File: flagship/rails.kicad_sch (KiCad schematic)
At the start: 58 parts, among them U5 TPS54560B 12V, U6 TPS54560B 5V, U7 TPS54560B 3V3

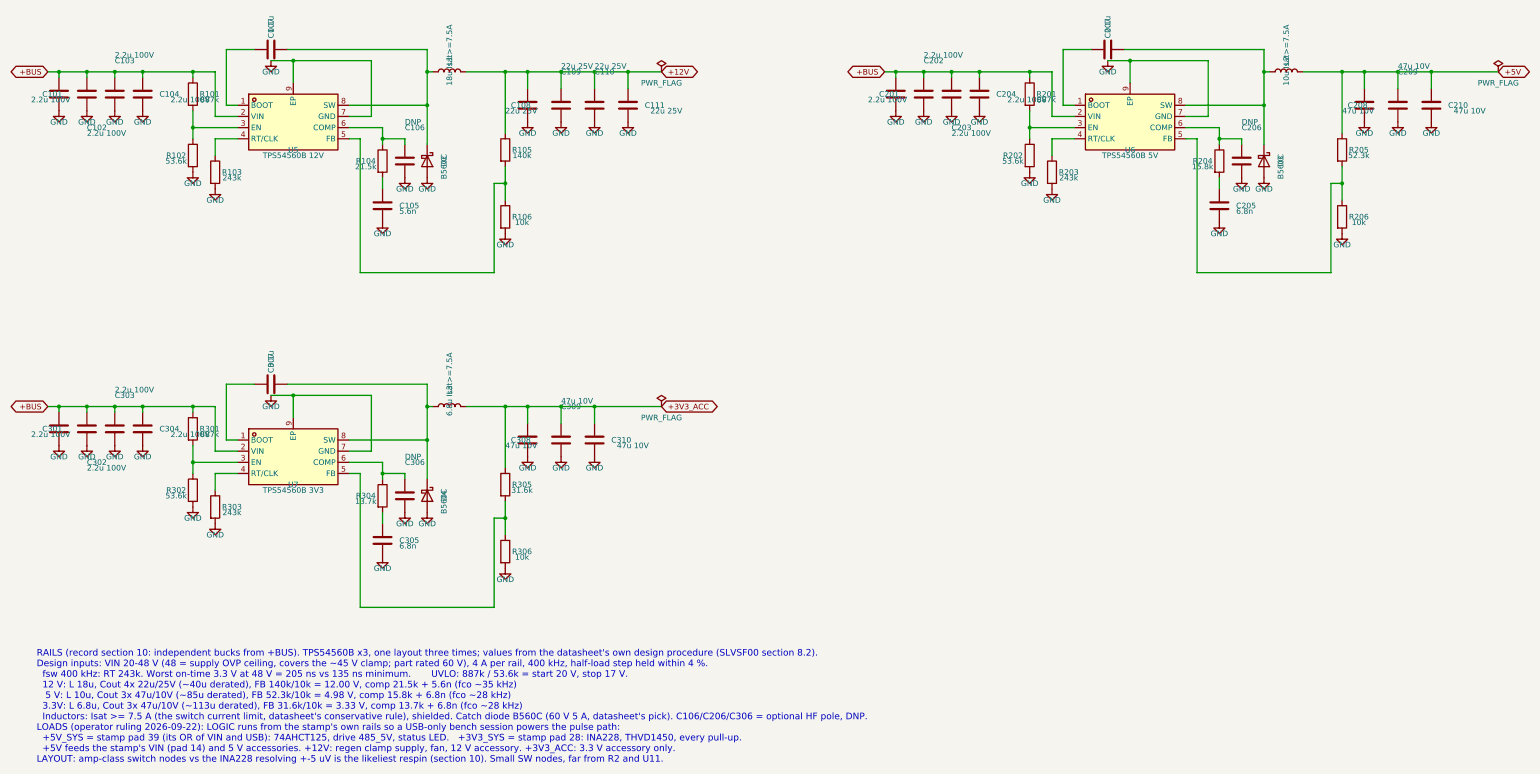
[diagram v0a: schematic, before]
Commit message: flagship: Kelvin WSK2512 shunts everywhere (LTC4364 sense now 4-terminal), bulk and MLCC parts picked
R1 (LTC4364, 2.5 mOhm) becomes a 4-terminal shunt with SENSE and OUT on its Kelvin taps;
R1/R2/R401 all Vishay WSK2512 on the T2.21 mm footprint that value range needs. Bulk:
2x EEH-ZA1J101P 100 uF 63 V hybrid polymer + 2x GRM32ER72A225KA35L; buck input caps get
the same MLCC part number. Regen resistors labeled D2TO35M 24 R 2 %. Input nets verified
exact after regeneration; ERC 0 on every detailed sheet.

Co-Authored-By: Claude Opus 5.5 (1M context) <noreply@anthropic.com>
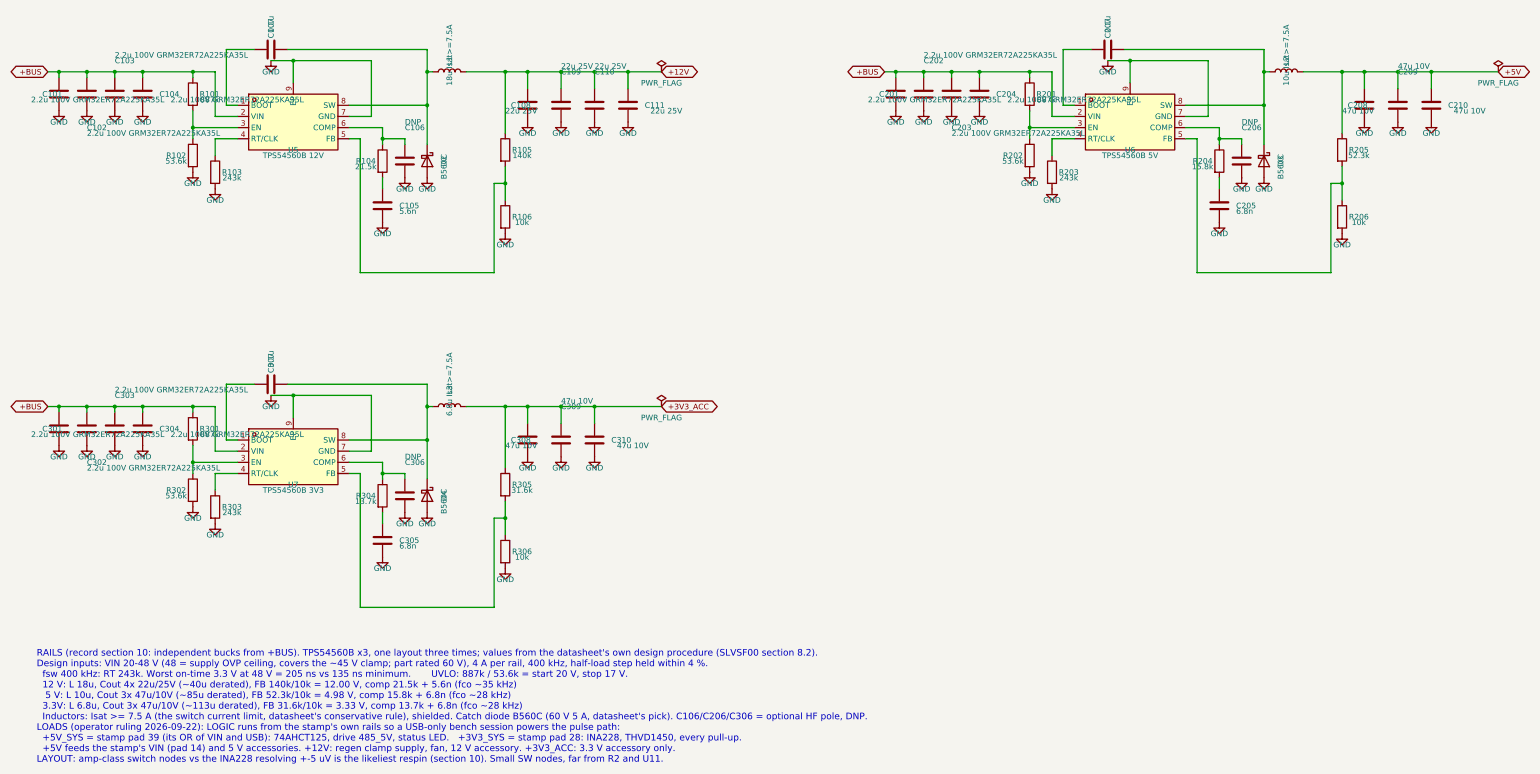
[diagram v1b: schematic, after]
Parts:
- C101, C102, C103, C104, C201, C202, C203, C204, C301, C302, C303, C304: value 2.2u 100V -> 2.2u 100V GRM32ER72A225KA35L
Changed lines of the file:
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@@
 		)
 		(property "Value" "0.1u"
-			(at 66.04 146.04999999999998 0)
+			(at 66.04 146.05 0)
 			(show_name no)
 			(do_not_autoplace no)
@@
 		)
 		(property "Value" "DNP"
-			(at 96.52 166.36999999999998 0)
+			(at 96.52 166.37 0)
 			(show_name no)
 			(do_not_autoplace no)
@@
 			)
 		)
-		(property "Value" "2.2u 100V"
-			(at 233.68 85.08999999999999 0)
+		(property "Value" "2.2u 100V GRM32ER72A225KA35L"
+			(at 233.68 85.09 0)
 			(show_name no)
 			(do_not_autoplace no)
@@
 		)
 		(property "Value" "TPS54560B 5V"
-			(at 261.62 97.78999999999999 0)
+			(at 261.62 97.79 0)
 			(show_name no)
 			(do_not_autoplace no)
@@
 			)
 		)
-		(property "Value" "2.2u 100V"
-			(at 11.43 85.08999999999999 0)
+		(property "Value" "2.2u 100V GRM32ER72A225KA35L"
+			(at 11.43 85.09 0)
 			(show_name no)
 			(do_not_autoplace no)
@@
 			)
 		)
-		(property "Value" "2.2u 100V"
+		(property "Value" "2.2u 100V GRM32ER72A225KA35L"
 			(at 30.48 151.13 0)
 			(show_name no)
@@
 			)
 		)
-		(property "Value" "2.2u 100V"
-			(at 43.18 161.29000000000002 0)
+		(property "Value" "2.2u 100V GRM32ER72A225KA35L"
+			(at 43.18 161.29 0)
 			(show_name no)
 			(do_not_autoplace no)
@@
 		)
 		(property "Value" "243k"
-			(at 57.15 179.07000000000002 0)
+			(at 57.15 179.07 0)
 			(show_name no)
 			(do_not_autoplace no)
@@
 		)
 		(property "Value" "887k"
-			(at 52.07 85.08999999999999 0)
+			(at 52.07 85.09 0)
 			(show_name no)
 			(do_not_autoplace no)
@@
 		)
 		(property "Value" "0.1u"
-			(at 66.04 69.85000000000001 0)
+			(at 66.04 69.85 0)
 			(show_name no)
 			(do_not_autoplace no)
@@
 		)
 		(property "Value" "52.3k"
-			(at 313.69 97.78999999999999 0)
+			(at 313.69 97.79 0)
 			(show_name no)
 			(do_not_autoplace no)
@@
 		)
 		(property "Value" "887k"
-			(at 242.57 85.08999999999999 0)
+			(at 242.57 85.09 0)
 			(show_name no)
 			(do_not_autoplace no)
@@
 			)
 		)
-		(property "Value" "2.2u 100V"
+		(property "Value" "2.2u 100V GRM32ER72A225KA35L"
 			(at 30.48 74.93 0)
 			(show_name no)
@@
 			)
 		)
-		(property "Value" "2.2u 100V"
-			(at 11.43 161.29000000000002 0)
+		(property "Value" "2.2u 100V GRM32ER72A225KA35L"
+			(at 11.43 161.29 0)
 			(show_name no)
 			(do_not_autoplace no)
@@
 		)
 		(property "Value" "887k"
-			(at 52.07 161.29000000000002 0)
+			(at 52.07 161.29 0)
 			(show_name no)
 			(do_not_autoplace no)
@@
 			)
 		)
-		(property "Value" "2.2u 100V"
+		(property "Value" "2.2u 100V GRM32ER72A225KA35L"
 			(at 24.13 168.91 0)
 			(show_name no)
@@
 		)
 		(property "Value" "10k"
-			(at 123.19 189.23000000000002 0)
+			(at 123.19 189.23 0)
 			(show_name no)
 			(do_not_autoplace no)
@@
 		)
 		(property "Value" "243k"
-			(at 247.65 102.86999999999999 0)
+			(at 247.65 102.87 0)
 			(show_name no)
 			(do_not_autoplace no)
@@
 			)
 		)
-		(property "Value" "2.2u 100V"
-			(at 201.93 85.08999999999999 0)
+		(property "Value" "2.2u 100V GRM32ER72A225KA35L"
+			(at 201.93 85.09 0)
 			(show_name no)
 			(do_not_autoplace no)
@@
 		)
 		(property "Value" "243k"
-			(at 57.15 102.86999999999999 0)
+			(at 57.15 102.87 0)
 			(show_name no)
 			(do_not_autoplace no)
@@
 			)
 		)
-		(property "Value" "2.2u 100V"
+		(property "Value" "2.2u 100V GRM32ER72A225KA35L"
 			(at 214.63 74.93 0)
 			(show_name no)
@@
 		)
 		(property "Value" "0.1u"
-			(at 256.54 69.85000000000001 0)
+			(at 256.54 69.85 0)
 			(show_name no)
 			(do_not_autoplace no)
@@
 			)
 		)
-		(property "Value" "2.2u 100V"
+		(property "Value" "2.2u 100V GRM32ER72A225KA35L"
 			(at 220.98 92.71 0)
 			(show_name no)
@@
 		)
 		(property "Value" "6.8u Isat>=7.5A"
-			(at 106.68 149.85999999999999 0)
+			(at 106.68 149.86 0)
 			(show_name no)
 			(do_not_autoplace no)
@@
 		)
 		(property "Value" "TPS54560B 12V"
-			(at 71.12 97.78999999999999 0)
+			(at 71.12 97.79 0)
 			(show_name no)
 			(do_not_autoplace no)
@@
 		)
 		(property "Value" "53.6k"
-			(at 44.45 175.26000000000002 0)
+			(at 44.45 175.26 0)
 			(show_name no)
 			(do_not_autoplace no)
@@
 		)
 		(property "Value" "140k"
-			(at 123.19 97.78999999999999 0)
+			(at 123.19 97.79 0)
 			(show_name no)
 			(do_not_autoplace no)
@@
 			)
 		)
-		(property "Value" "2.2u 100V"
+		(property "Value" "2.2u 100V GRM32ER72A225KA35L"
 			(at 24.13 92.71 0)
 			(show_name no)
@@
 			)
 		)
-		(property "Value" "2.2u 100V"
-			(at 43.18 85.08999999999999 0)
+		(property "Value" "2.2u 100V GRM32ER72A225KA35L"
+			(at 43.18 85.09 0)
 			(show_name no)
 			(do_not_autoplace no)
